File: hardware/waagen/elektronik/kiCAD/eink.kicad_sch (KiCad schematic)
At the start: 1 part, among them J6 Conn_01x08

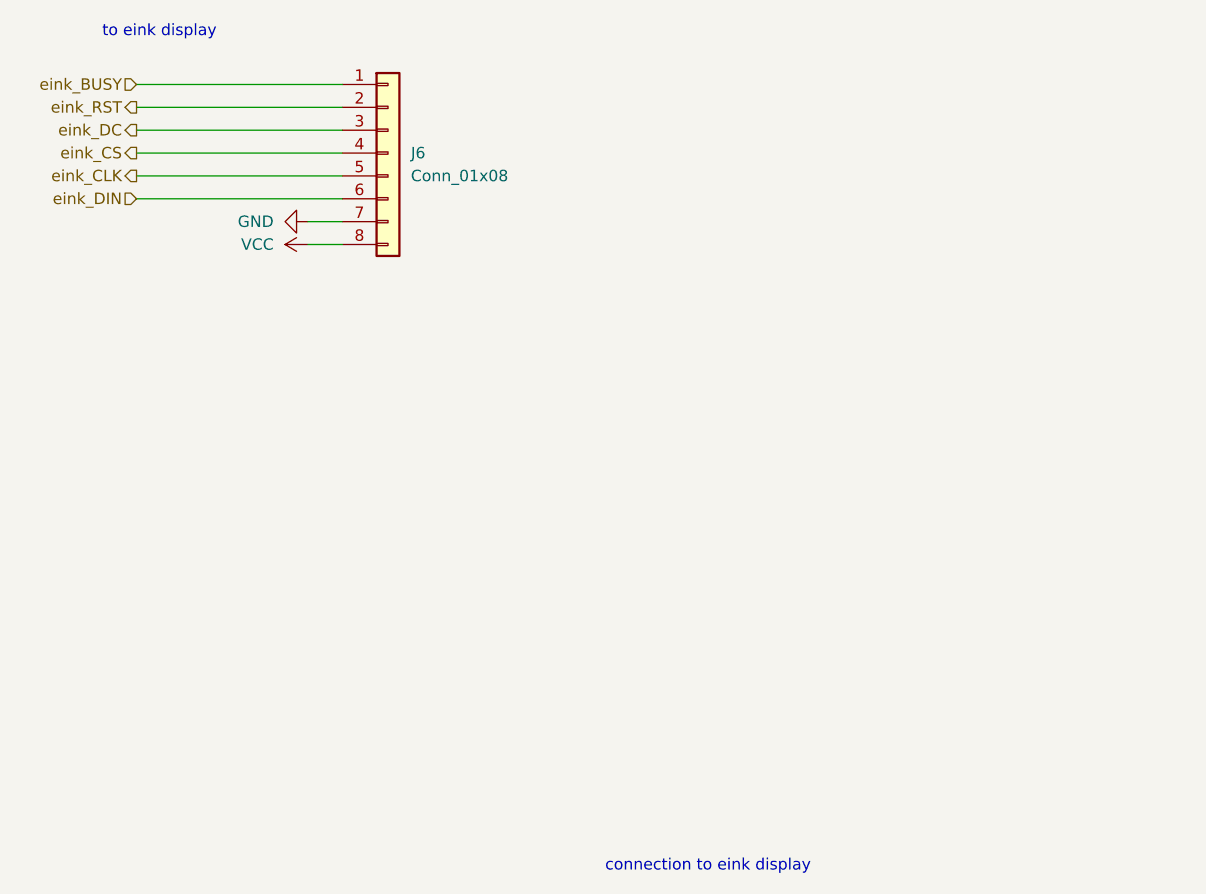
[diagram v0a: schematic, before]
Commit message: second LDO for eink added
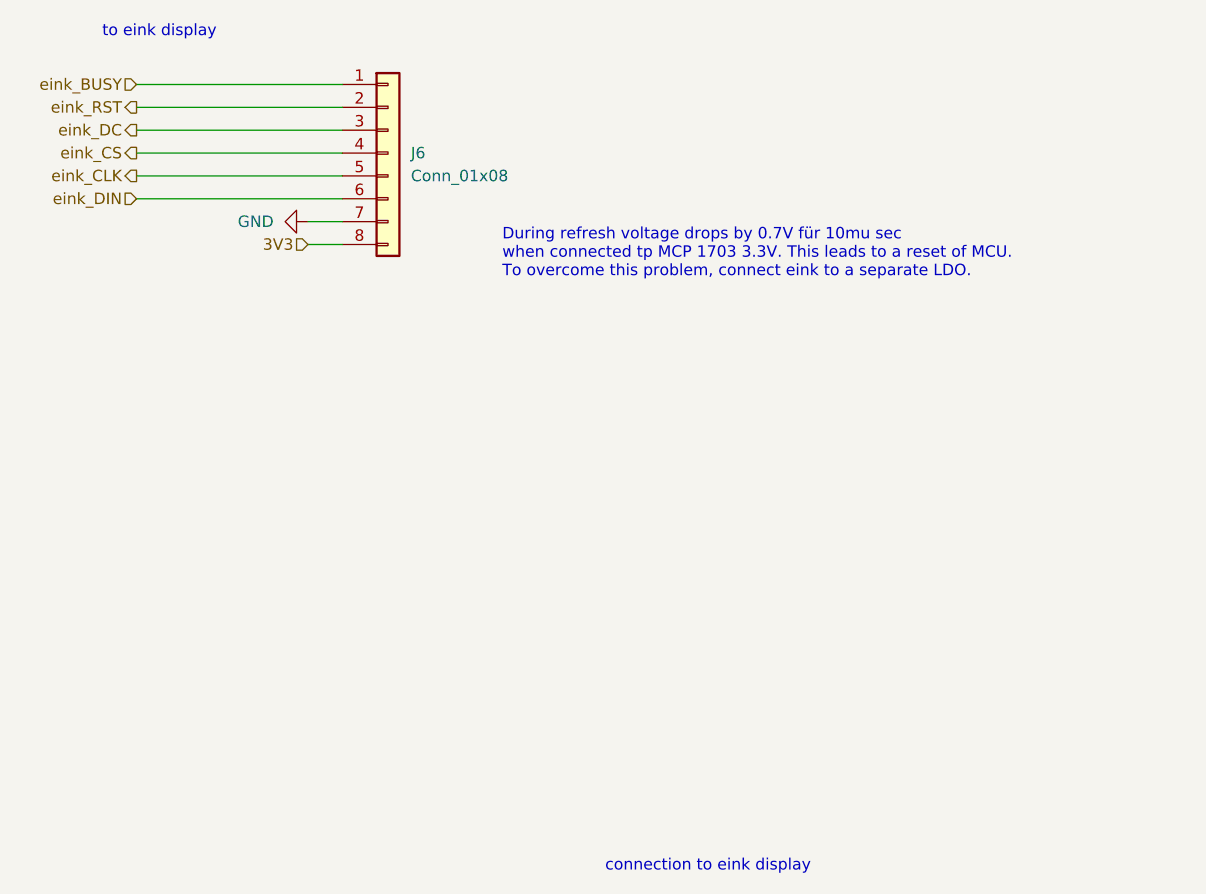
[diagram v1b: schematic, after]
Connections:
- net VCC renamed 3V3
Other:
- note added: "During refresh voltage drops by 0.7V für 10mu sec when connected tp MCP 1703 3.3V. This leads to a reset of MCU. To overcome this problem, connect eink to a separate LDO."
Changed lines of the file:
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@@
+    (effects (font (size 1.27 1.27)) (justify left bottom))
+  )
+  (text "During refresh voltage drops by 0.7V für 10mu sec \nwhen connected tp MCP 1703 3.3V. This leads to a reset of MCU.\nTo overcome this problem, connect eink to a separate LDO."
+    (at 170.18 106.68 0)
     (effects (font (size 1.27 1.27)) (justify left bottom))
   )
   (text "connection to eink display" (at 181.61 172.72 0)
     (effects (font (size 1.27 1.27)) (justify left bottom))
+  )
+  (hierarchical_label "3V3" (shape input) (at 148.59 102.87 180)
+    (effects (font (size 1.27 1.27)) (justify right))
   )
   (hierarchical_label "eink_RST" (shape output) (at 129.54 87.63 180)
@@
     (effects (font (size 1.27 1.27)) (justify right))
   )
-  (symbol (lib_id "power:VCC") (at 148.59 102.87 90) (unit 1)
-    (in_bom yes) (on_board yes) (fields_autoplaced)
-    (property "Reference" "#PWR041" (id 0) (at 152.4 102.87 0)
-      (effects (font (size 1.27 1.27)) hide)
-    )
-    (property "Value" "VCC" (id 1) (at 144.78 102.8699 90)
-      (effects (font (size 1.27 1.27)) (justify left))
-    )
-    (property "Footprint" "" (id 2) (at 148.59 102.87 0)
-      (effects (font (size 1.27 1.27)) hide)
-    )
-    (property "Datasheet" "" (id 3) (at 148.59 102.87 0)
-      (effects (font (size 1.27 1.27)) hide)
-    )
-    (pin "1")
-  )
   (symbol (lib_id "Connector_Generic:Conn_01x08") (at 157.48 92.71 0) (unit 1)

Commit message: JP1 added
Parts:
- added JP1: SolderJumper_2_Open, Jumper:SolderJumper-2_P1.3mm_Open_RoundedPad1.0x1.5mm, symbol Jumper:SolderJumper_2_Open
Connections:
- net 3V3: now also JP1.2 (B)
- new net VCC: JP1.1 (A)
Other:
- note added: "Close this jumper, when powering the eink display via standard VCC. Ensure second LDO is not placed in this case."
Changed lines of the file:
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@@
 (kicad_sch (version 20211123) (generator eeschema)
   (paper "A4")
+  (junction (at 151.13 102.87) (diameter 0) (color 0 0 0 0)
+  )
+  (wire (pts (xy 139.7 113.03) (xy 142.24 113.03))
+    (stroke (width 0) (type default) (color 0 0 0 0))
+  )
   (wire (pts (xy 129.54 92.71) (xy 152.4 92.71))
     (stroke (width 0) (type default) (color 0 0 0 0))
@@
     (stroke (width 0) (type default) (color 0 0 0 0))
   )
-  (wire (pts (xy 148.59 102.87) (xy 152.4 102.87))
+  (wire (pts (xy 148.59 102.87) (xy 151.13 102.87))
     (stroke (width 0) (type default) (color 0 0 0 0))
   )
   (wire (pts (xy 129.54 85.09) (xy 152.4 85.09))
+    (stroke (width 0) (type default) (color 0 0 0 0))
+  )
+  (wire (pts (xy 149.86 113.03) (xy 151.13 113.03))
+    (stroke (width 0) (type default) (color 0 0 0 0))
+  )
+  (wire (pts (xy 151.13 102.87) (xy 152.4 102.87))
     (stroke (width 0) (type default) (color 0 0 0 0))
   )
@@
     (stroke (width 0) (type default) (color 0 0 0 0))
   )
+  (wire (pts (xy 151.13 102.87) (xy 151.13 113.03))
+    (stroke (width 0) (type default) (color 0 0 0 0))
+  )
   (text "to eink display" (at 125.73 80.01 0)
+    (effects (font (size 1.27 1.27)) (justify left bottom))
+  )
+  (text "Close this jumper, when powering the eink display\nvia standard VCC. Ensure second LDO is not placed\nin this case."
+    (at 120.65 121.92 0)
     (effects (font (size 1.27 1.27)) (justify left bottom))
   )
@@
     (effects (font (size 1.27 1.27)) (justify right))
   )
+  (symbol (lib_id "Jumper:SolderJumper_2_Open") (at 146.05 113.03 0) (unit 1)
+    (in_bom yes) (on_board yes) (fields_autoplaced)
+    (property "Reference" "JP1" (id 0) (at 146.05 106.68 0))
+    (property "Value" "SolderJumper_2_Open" (id 1) (at 146.05 109.22 0))
+    (property "Footprint" "Jumper:SolderJumper-2_P1.3mm_Open_RoundedPad1.0x1.5mm" (id 2) (at 146.05 113.03 0)
+      (effects (font (size 1.27 1.27)) hide)
+    )
+    (property "Datasheet" "~" (id 3) (at 146.05 113.03 0)
+      (effects (font (size 1.27 1.27)) hide)
+    )
+    (pin "1")
+    (pin "2")
+  )
+  (symbol (lib_id "power:VCC") (at 139.7 113.03 90) (unit 1)
+    (in_bom yes) (on_board yes) (fields_autoplaced)
+    (property "Reference" "#PWR047" (id 0) (at 143.51 113.03 0)
+      (effects (font (size 1.27 1.27)) hide)
+    )
+    (property "Value" "VCC" (id 1) (at 135.89 113.0299 90)
+      (effects (font (size 1.27 1.27)) (justify left))
+    )
+    (property "Footprint" "" (id 2) (at 139.7 113.03 0)
+      (effects (font (size 1.27 1.27)) hide)
+    )
+    (property "Datasheet" "" (id 3) (at 139.7 113.03 0)
+      (effects (font (size 1.27 1.27)) hide)
+    )
+    (pin "1")
+  )
   (symbol (lib_id "Connector_Generic:Conn_01x08") (at 157.48 92.71 0) (unit 1)

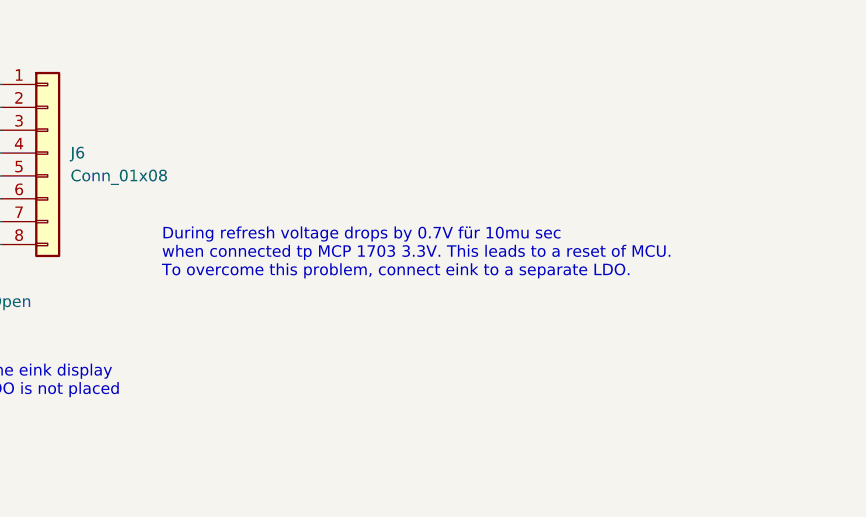
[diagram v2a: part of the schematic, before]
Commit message: Error on JP1 fixed and changed scale wires pads
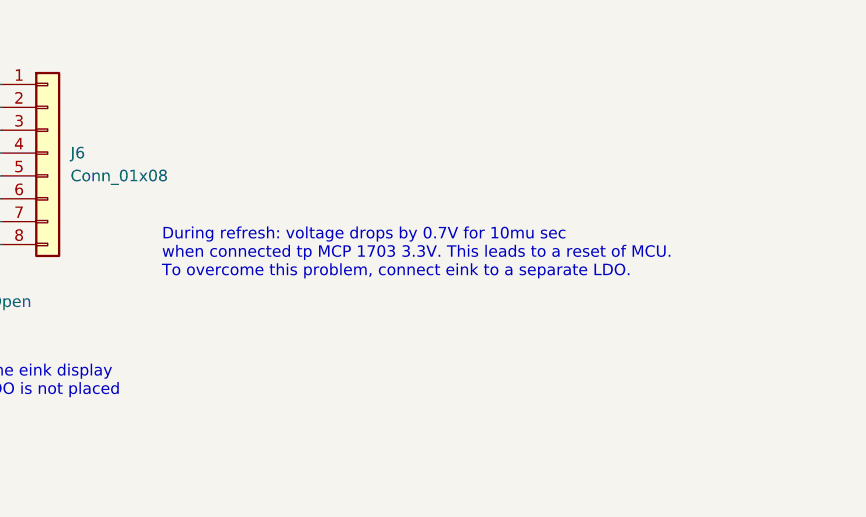
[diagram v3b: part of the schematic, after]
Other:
- note added: "During refresh: voltage drops by 0.7V for 10mu sec when connected tp MCP 1703 3.3V. This leads to a reset of MCU. To overcome this problem, connect eink to a separate LDO."
- note removed: "During refresh voltage drops by 0.7V für 10mu sec when connected tp MCP 1703 3.3V. This leads to a reset of MCU. To overcome this problem, connect eink to a separate LDO."
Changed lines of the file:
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@@
     (effects (font (size 1.27 1.27)) (justify left bottom))
   )
-  (text "During refresh voltage drops by 0.7V für 10mu sec \nwhen connected tp MCP 1703 3.3V. This leads to a reset of MCU.\nTo overcome this problem, connect eink to a separate LDO."
+  (text "During refresh: voltage drops by 0.7V for 10mu sec \nwhen connected tp MCP 1703 3.3V. This leads to a reset of MCU.\nTo overcome this problem, connect eink to a separate LDO."
     (at 170.18 106.68 0)
     (effects (font (size 1.27 1.27)) (justify left bottom))
